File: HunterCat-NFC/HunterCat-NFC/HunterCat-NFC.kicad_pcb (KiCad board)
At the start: 4 copper layers, 80.7 x 33.5 mm, 72 parts, among them J1 Battery, J2 Conn_01x06_Female, P1 USB_C_Plug_USB2.0, Q1 DMG3415U-7, U1 ATSAMD21E18A, U2 PN7150B0HN_C11002E-PN7150B0HN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, U3 MCP73831-3-OT, U4 AP2112K-3.3, U5 GD25Q16CEIGR, Y1 27.12Mhz

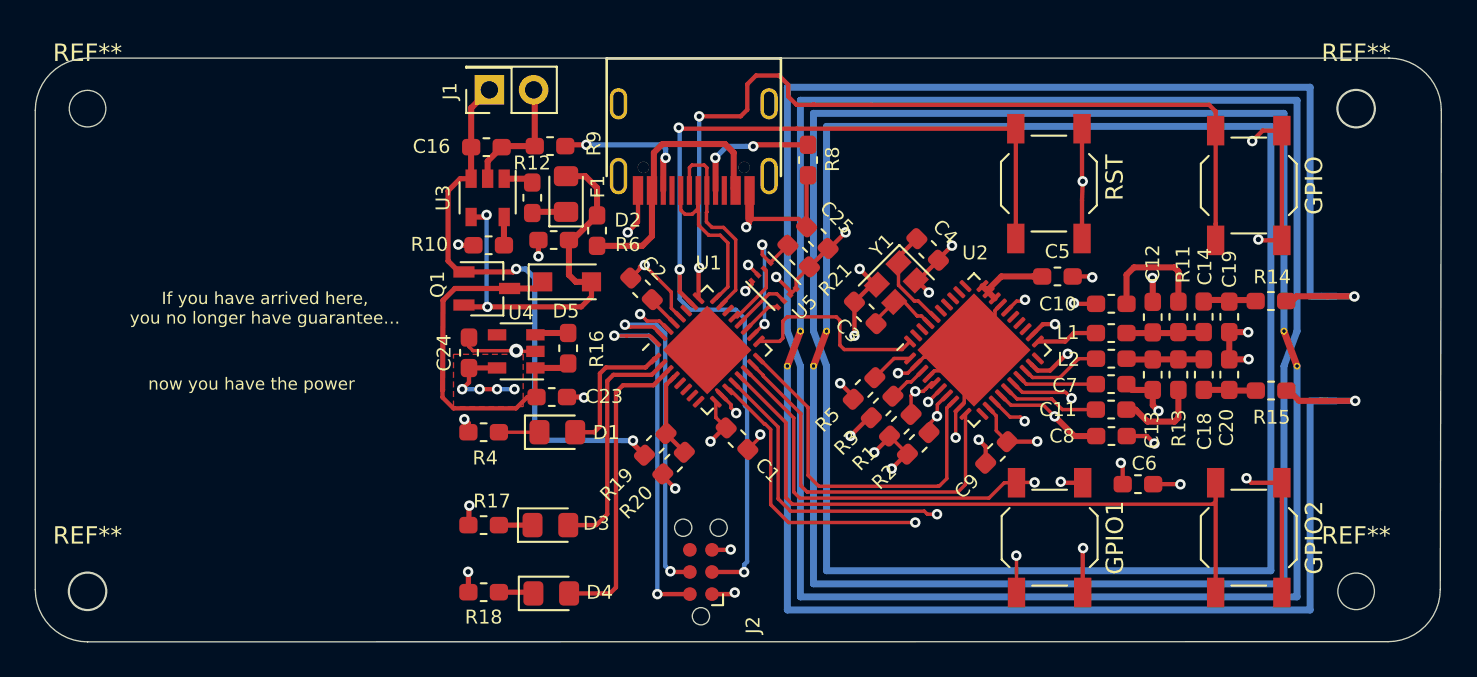
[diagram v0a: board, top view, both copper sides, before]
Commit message: modify coil holes
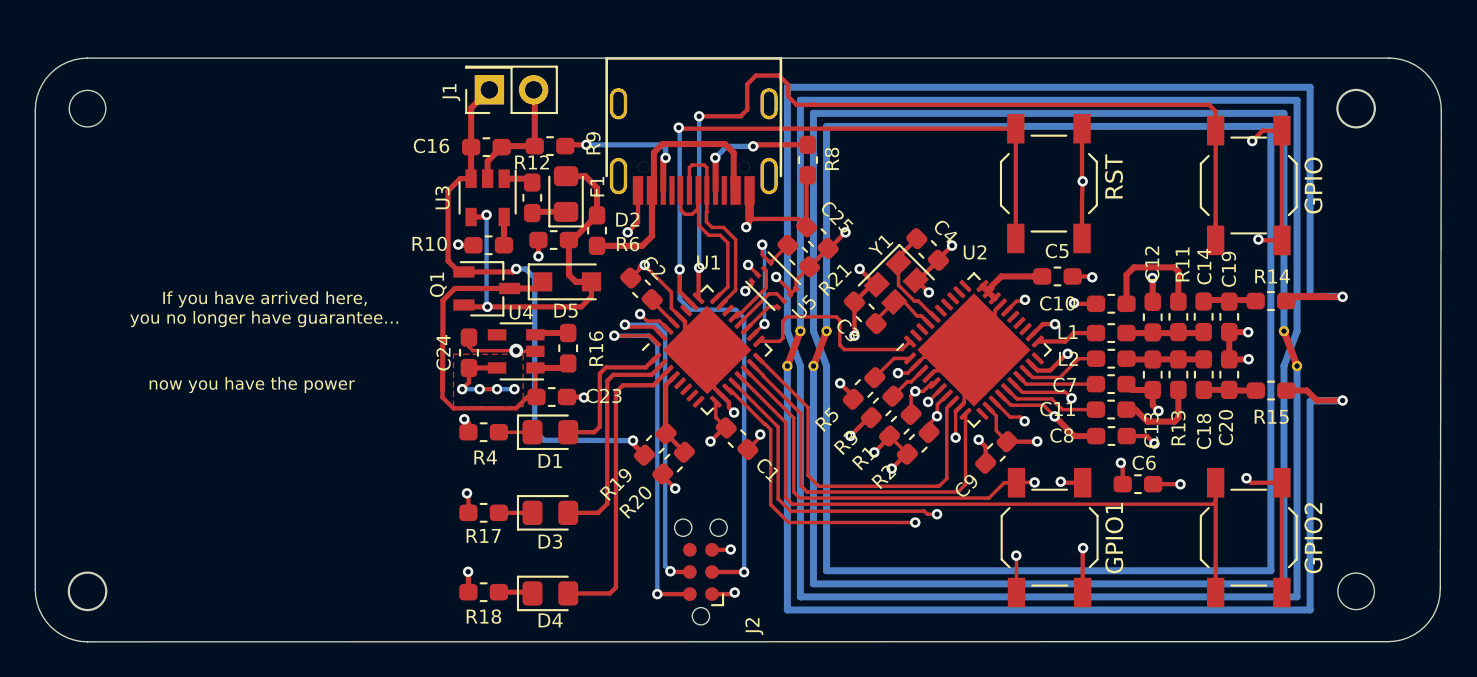
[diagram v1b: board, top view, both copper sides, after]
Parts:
- moved D3 0.70 mm to (109.6, 101.6)
- moved R17 0.70 mm to (105.7, 101.6)
- moved D1 0.40 mm to (109.6, 97.0)
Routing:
- net GND: track 117.2 -> 122.7 mm
- net Net-(L3-Pad1): track 5.88 -> 8.06 mm
- net Net-(L3-Pad2): track 6.56 -> 4.58 mm
- net /LED2: track 13.7 -> 13.0 mm

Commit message: update PCB
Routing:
- net /IRQ: track 20.8 -> 17.9 mm
- net /GPIO2: track 40.2 -> 37.7 mm
- net /SDA: track 26.7 -> 24.2 mm
- net /GPIO1: track 29.7 -> 27.2 mm
- net /SCL: track 25.4 -> 22.9 mm
- net /VEN: track 21.9 -> 19.5 mm
- net (no net): track 0.00 -> 0.65 mm
- net /CS: track 8.19 -> 8.82 mm
- net GND: track 122.7 -> 122.4 mm, vias 38 -> 39

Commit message: update v1.1 2 layes
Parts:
- removed G***: LOGO, Aesthetics:electronic_cats_logo_8x6
- removed REF** (x2): MountingHole_2.2mm_M2, MountingHole:MountingHole_2.2mm_M2
- removed REF** (x4): MountingHole_2.1mm, MountingHole:MountingHole_2.1mm
- removed REF**: OSHW-Logo_5.7x6mm_SilkScreen, Symbol:OSHW-Logo_5.7x6mm_SilkScreen
- Q1: footprint Package_TO_SOT_SMD:TSOT-23 -> Package_TO_SOT_SMD:SOT-23
- moved C1 4.73 mm to (116.3, 99.8), turned to 225 degrees
- moved C25 2.57 mm to (122.5, 86.6)
- moved U5 2.53 mm to (119.8, 88.0)
- moved R21 2.53 mm to (121.4, 87.7)
- moved U1 2.49 mm to (116.2, 93.0)
- moved J2 1.90 mm to (116.3, 105.1), turned to 0 degrees
- moved R20 1.41 mm to (115.2, 98.8)
- moved R19 1.41 mm to (114.2, 97.7)
- moved C2 1.02 mm to (114.4, 87.8), turned to 0 degrees
- moved C9 0.72 mm to (135.3, 97.4)
- moved Q1 0.18 mm to (106.1, 88.7), turned to 90 degrees
- renumbered RST to SW1, GPIO1 to SW2, GPIO2 to SW3, GPIO to SW4
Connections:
- C9 pad 1: +BATT -> +3V3
- Q1 pad 1: +BATT -> VBUS
- Q1 pad 2: VBUS -> Net-(C23-Pad1)
- Q1 pad 3: Net-(C23-Pad1) -> +BATT
- U2 pad 12: +BATT -> +3V3
- U2 pad 26: +BATT -> +3V3
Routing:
- net GND: track 122.4 -> 268.8 mm, vias 39 -> 43
- net +3V3: track 27.9 -> 130.6 mm, vias 15 -> 17
- net +BATT: track 46.3 -> 55.9 mm, vias 4 -> 2
- net /SCL: track 22.9 -> 29.1 mm
- net /SWCLK: track 19.8 -> 25.8 mm
- net /IRQ: track 17.9 -> 23.5 mm
- net /RST: track 58.4 -> 63.9 mm
- net /SDA: track 24.2 -> 29.4 mm
- net /VEN: track 19.5 -> 24.6 mm
- net /GPIO2: track 37.7 -> 42.7 mm
- net /GPIO1: track 27.2 -> 32.1 mm
- net /GPIO: track 50.7 -> 47.0 mm, vias 2 -> 5
- net /LED2: track 13.0 -> 9.61 mm
- net /LED3: track 17.5 -> 14.4 mm
- net /LED1: track 8.14 -> 5.47 mm
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- added copper zone on B.Cu, net GND
- added copper zone on F.Cu, net GND
- removed copper zone on In2.Cu, net +3V3
- removed copper zone on In2.Cu, net +BATT
- removed copper zone on In1.Cu, net GND
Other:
- copper layers 4 -> 2
- board text added: "V1.1"
- board text removed: "V1.0"

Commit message: fiz silk and layout
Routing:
- net GND: track 268.8 -> 279.6 mm
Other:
- board text added: "+"
- board text added: "."
